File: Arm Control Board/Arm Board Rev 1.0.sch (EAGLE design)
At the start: 54 parts

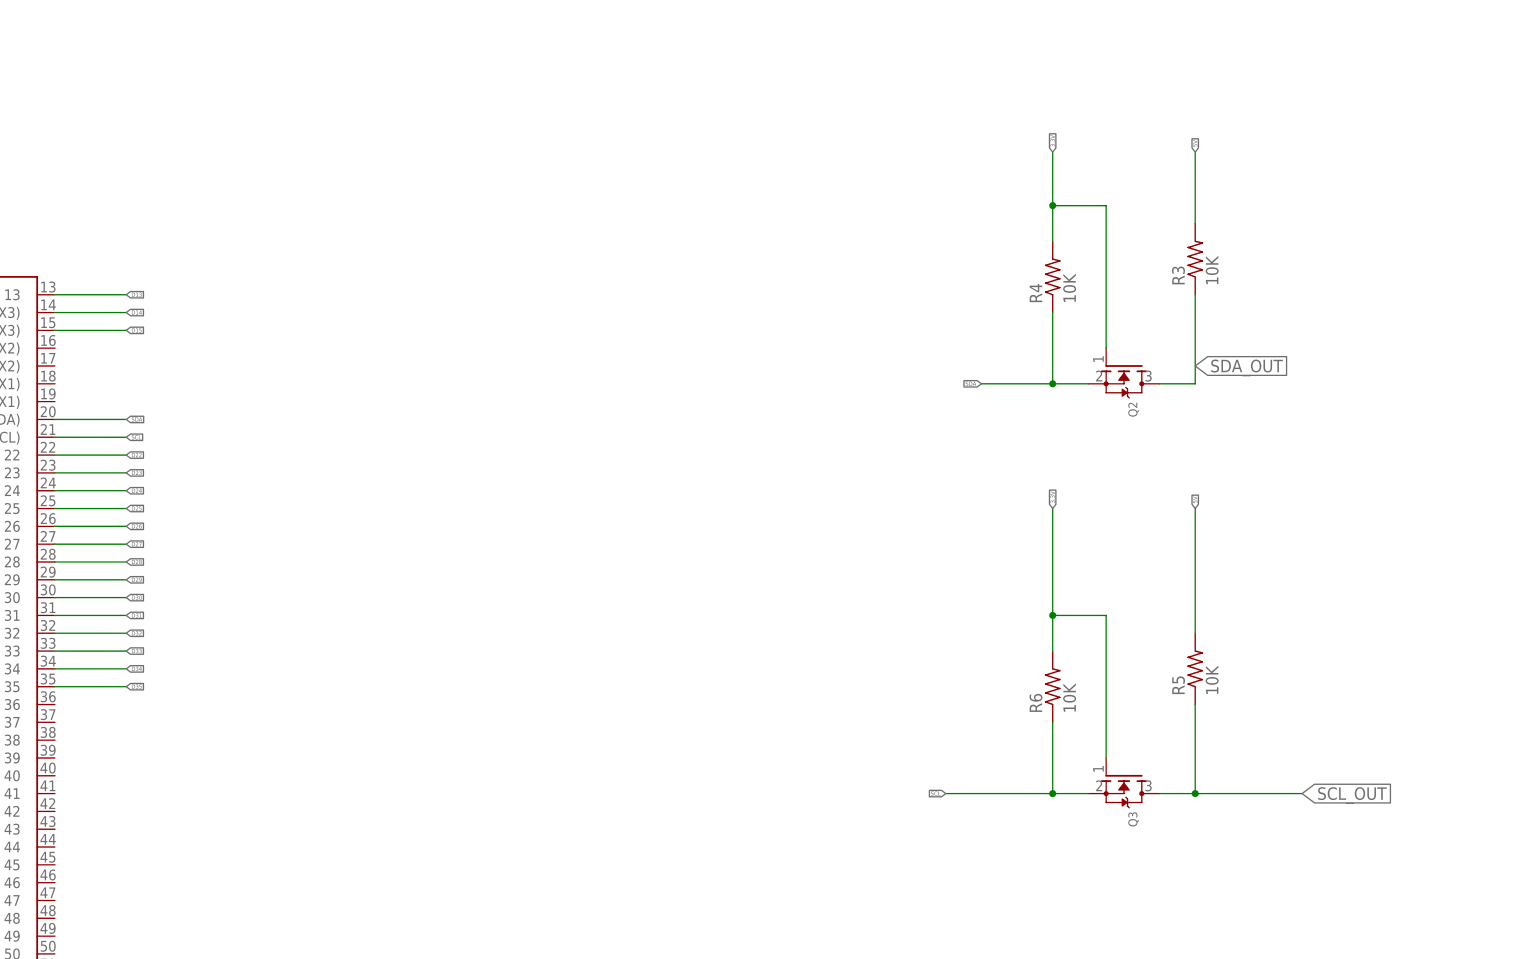
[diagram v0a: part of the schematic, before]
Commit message: added pull up resistors for i2c
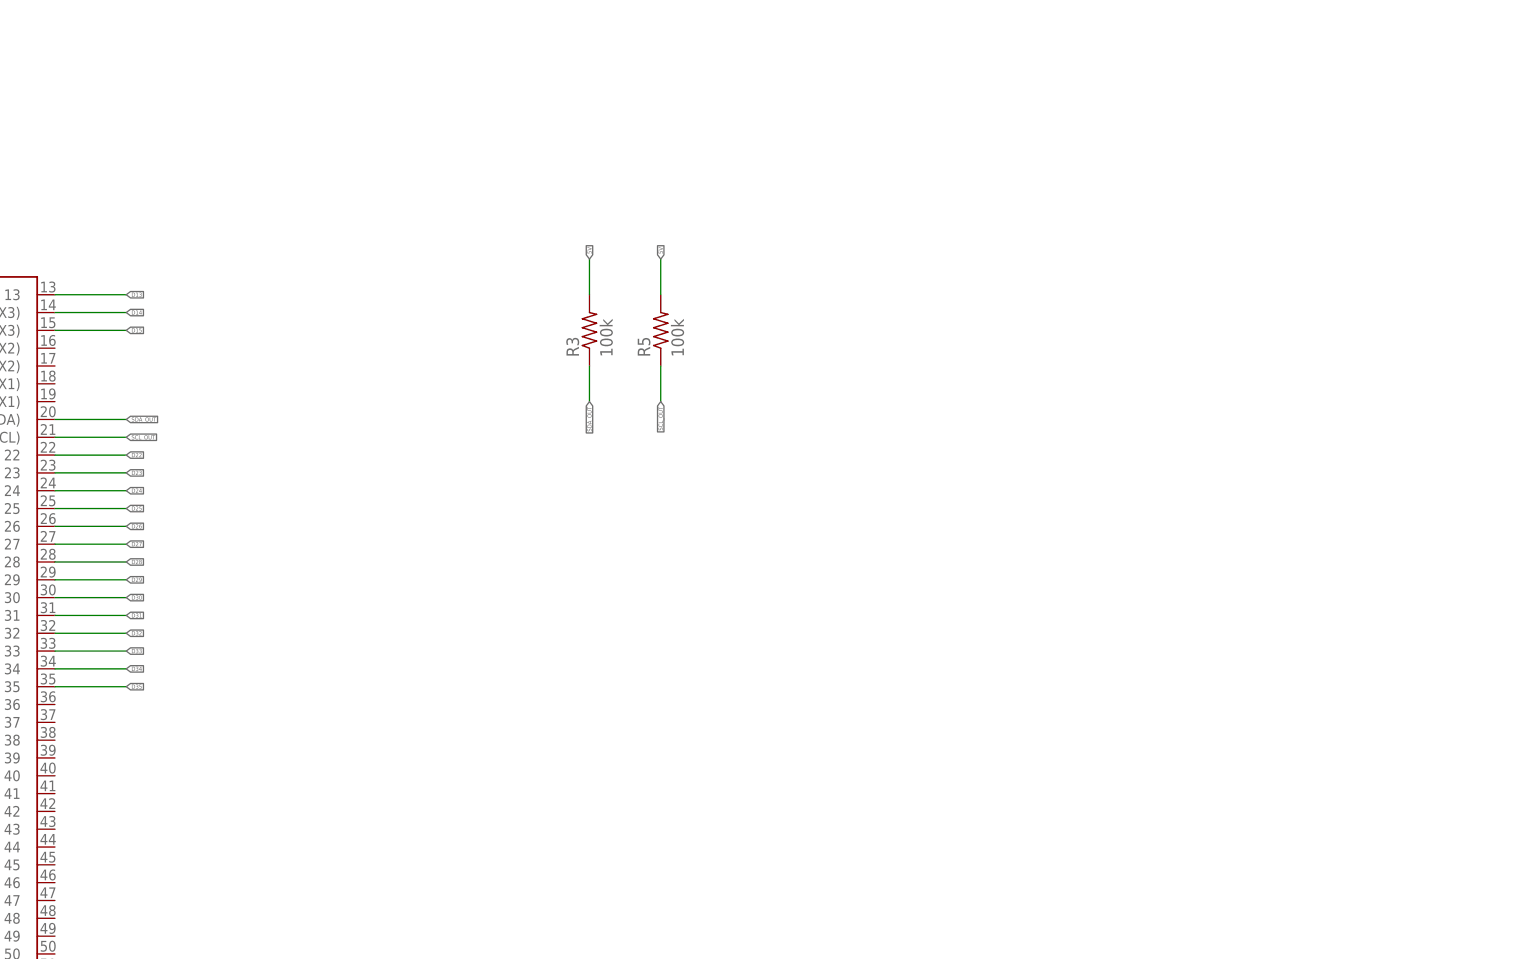
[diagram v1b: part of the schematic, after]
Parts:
- removed Q2, Q3: (no value), adafruit:MOSFET-NREFLOW
- removed R4, R6: 10K, rcl:R-US_R0603
- R3, R5: value 10K -> 100k; device rcl:R-US_R0603 -> rcl:R-US_0204/2V
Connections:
- removed net SCL: B1.21(SCL), Q3.S, R6.1
- removed net SDA: B1.20(SDA), Q2.S, R4.1
- net 3.3V: no longer Q2.G, Q3.G, R4.2, R6.2
- net SCL_OUT: now also B1.21(SCL); no longer Q3.D
- net SDA_OUT: now also B1.20(SDA); no longer Q2.D
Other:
- moved on the sheet: R3, R5

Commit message: removed tx and rx
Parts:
- removed Q13, Q14: (no value), adafruit:MOSFET-NREFLOW
- removed R25, R26, R27, R28: 10K, rcl:R-US_R0603
- removed RX: \, wirepad:3,81/1,1
- removed TX: (no value), wirepad:3,81/1,1
- R3, R5: value 100k -> 100K
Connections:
- removed net N$1: Q14.S, R28.1, RX.P
- removed net N$2: Q13.S, R26.1, TX.P
- net 3.3V: no longer Q13.G, Q14.G, R26.2, R28.2
- net 5V: no longer R25.2, R27.2
- net RX: no longer Q13.D, R25.1
- net TX: no longer Q14.D, R27.1
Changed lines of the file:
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@@
 </classes>
 <parts>
-<part name="TX" library="wirepad" deviceset="3,81/1,1" device=""/>
-<part name="RX" library="wirepad" deviceset="3,81/1,1" device="" value="\"/>
-<part name="Q13" library="adafruit" deviceset="MOSFET-N" device="REFLOW"/>
-<part name="R25" library="rcl" deviceset="R-US_" device="R0603" value="10K"/>
-<part name="R26" library="rcl" deviceset="R-US_" device="R0603" value="10K"/>
-<part name="Q14" library="adafruit" deviceset="MOSFET-N" device="REFLOW"/>
-<part name="R27" library="rcl" deviceset="R-US_" device="R0603" value="10K"/>
-<part name="R28" library="rcl" deviceset="R-US_" device="R0603" value="10K"/>
 <part name="12V" library="wirepad" deviceset="3,81/1,4" device=""/>
 <part name="GND" library="wirepad" deviceset="3,81/1,4" device=""/>
@@
 <part name="ENCODER_OUTPUT1" library="con-lstb" deviceset="MA04-1" device=""/>
 <part name="B1" library="SparkFun-Boards" library_urn="urn:adsk.eagle:library:509" deviceset="ARDUINO_MEGA_R3" device="FULL" package3d_urn="urn:adsk.eagle:package:37320/1"/>
-<part name="R3" library="rcl" library_urn="urn:adsk.eagle:library:334" deviceset="R-US_" device="0204/2V" package3d_urn="urn:adsk.eagle:package:23495/1" value="100k"/>
-<part name="R5" library="rcl" library_urn="urn:adsk.eagle:library:334" deviceset="R-US_" device="0204/2V" package3d_urn="urn:adsk.eagle:package:23495/1" value="100k"/>
+<part name="R3" library="rcl" library_urn="urn:adsk.eagle:library:334" deviceset="R-US_" device="0204/2V" package3d_urn="urn:adsk.eagle:package:23495/1" value="100K"/>
+<part name="R5" library="rcl" library_urn="urn:adsk.eagle:library:334" deviceset="R-US_" device="0204/2V" package3d_urn="urn:adsk.eagle:package:23495/1" value="100K"/>
 </parts>
 <sheets>
@@
 </plain>
 <instances>
-<instance part="TX" gate="P" x="25.4" y="60.96" smashed="yes">
-<attribute name="NAME" x="24.257" y="62.8142" size="1.778" layer="95"/>
-<attribute name="VALUE" x="24.257" y="57.658" size="1.778" layer="96"/>
-</instance>
-<instance part="RX" gate="P" x="25.4" y="33.02" smashed="yes">
-<attribute name="NAME" x="24.257" y="34.8742" size="1.778" layer="95"/>
-<attribute name="VALUE" x="24.257" y="29.718" size="1.778" layer="96"/>
-</instance>
-<instance part="Q13" gate="G$1" x="71.12" y="63.5" smashed="yes" rot="R270">
-<attribute name="NAME" x="71.755" y="58.42" size="1.27" layer="95" rot="R270"/>
-<attribute name="VALUE" x="69.85" y="58.42" size="1.27" layer="96" rot="R270"/>
-</instance>
-<instance part="R25" gate="G$1" x="81.28" y="78.74" smashed="yes" rot="R90">
-<attribute name="NAME" x="79.7814" y="74.93" size="1.778" layer="95" rot="R90"/>
-<attribute name="VALUE" x="84.582" y="74.93" size="1.778" layer="96" rot="R90"/>
-</instance>
-<instance part="R26" gate="G$1" x="60.96" y="76.2" smashed="yes" rot="R90">
-<attribute name="NAME" x="59.4614" y="72.39" size="1.778" layer="95" rot="R90"/>
-<attribute name="VALUE" x="64.262" y="72.39" size="1.778" layer="96" rot="R90"/>
-</instance>
-<instance part="Q14" gate="G$1" x="149.86" y="35.56" smashed="yes" rot="R270">
-<attribute name="NAME" x="150.495" y="30.48" size="1.27" layer="95" rot="R270"/>
-<attribute name="VALUE" x="148.59" y="30.48" size="1.27" layer="96" rot="R270"/>
-</instance>
-<instance part="R27" gate="G$1" x="160.02" y="50.8" smashed="yes" rot="R90">
-<attribute name="NAME" x="158.5214" y="46.99" size="1.778" layer="95" rot="R90"/>
-<attribute name="VALUE" x="163.322" y="46.99" size="1.778" layer="96" rot="R90"/>
-</instance>
-<instance part="R28" gate="G$1" x="139.7" y="48.26" smashed="yes" rot="R90">
-<attribute name="NAME" x="138.2014" y="44.45" size="1.778" layer="95" rot="R90"/>
-<attribute name="VALUE" x="143.002" y="44.45" size="1.778" layer="96" rot="R90"/>
-</instance>
 <instance part="12V" gate="1" x="0" y="342.9" smashed="yes">
 <attribute name="NAME" x="-1.143" y="344.7542" size="1.778" layer="95"/>
@@
 </busses>
 <nets>
-<net name="N$1" class="0">
-<segment>
-<pinref part="RX" gate="P" pin="P"/>
-<wire x1="27.94" y1="33.02" x2="139.7" y2="33.02" width="0.1524" layer="91"/>
-<pinref part="Q14" gate="G$1" pin="S"/>
-<pinref part="R28" gate="G$1" pin="1"/>
-<wire x1="139.7" y1="33.02" x2="144.78" y2="33.02" width="0.1524" layer="91"/>
-<wire x1="139.7" y1="43.18" x2="139.7" y2="33.02" width="0.1524" layer="91"/>
-<junction x="139.7" y="33.02"/>
-</segment>
-</net>
-<net name="N$2" class="0">
-<segment>
-<pinref part="Q13" gate="G$1" pin="S"/>
-<pinref part="TX" gate="P" pin="P"/>
-<wire x1="27.94" y1="60.96" x2="60.96" y2="60.96" width="0.1524" layer="91"/>
-<pinref part="R26" gate="G$1" pin="1"/>
-<wire x1="60.96" y1="60.96" x2="66.04" y2="60.96" width="0.1524" layer="91"/>
-<wire x1="60.96" y1="71.12" x2="60.96" y2="60.96" width="0.1524" layer="91"/>
-<junction x="60.96" y="60.96"/>
-</segment>
-</net>
 <net name="5V" class="0">
-<segment>
-<pinref part="R25" gate="G$1" pin="2"/>
-<wire x1="81.28" y1="83.82" x2="81.28" y2="99.06" width="0.1524" layer="91"/>
-<label x="81.28" y="99.06" size="0.6096" layer="95" rot="R90" xref="yes"/>
-</segment>
-<segment>
-<pinref part="R27" gate="G$1" pin="2"/>
-<wire x1="160.02" y1="55.88" x2="160.02" y2="71.12" width="0.1524" layer="91"/>
-<label x="160.02" y="71.12" size="0.6096" layer="95" rot="R90" xref="yes"/>
-</segment>
 <segment>
 <pinref part="ENCODER_OUTPUT" gate="1" pin="4"/>
@@
 </net>
 <net name="3.3V" class="0">
-<segment>
-<pinref part="Q13" gate="G$1" pin="G"/>
-<pinref part="R26" gate="G$1" pin="2"/>
-<wire x1="60.96" y1="86.36" x2="60.96" y2="81.28" width="0.1524" layer="91"/>
-<wire x1="68.58" y1="86.36" x2="60.96" y2="86.36" width="0.1524" layer="91"/>
-<wire x1="68.58" y1="86.36" x2="68.58" y2="66.04" width="0.1524" layer="91"/>
-<wire x1="60.96" y1="86.36" x2="60.96" y2="99.06" width="0.1524" layer="91"/>
-<junction x="60.96" y="86.36"/>
-<label x="60.96" y="99.06" size="0.6096" layer="95" rot="R90" xref="yes"/>
-</segment>
-<segment>
-<pinref part="Q14" gate="G$1" pin="G"/>
-<pinref part="R28" gate="G$1" pin="2"/>
-<wire x1="139.7" y1="58.42" x2="139.7" y2="53.34" width="0.1524" layer="91"/>
-<wire x1="147.32" y1="58.42" x2="139.7" y2="58.42" width="0.1524" layer="91"/>
-<wire x1="147.32" y1="58.42" x2="147.32" y2="38.1" width="0.1524" layer="91"/>
-<wire x1="139.7" y1="58.42" x2="139.7" y2="71.12" width="0.1524" layer="91"/>
-<junction x="139.7" y="58.42"/>
-<label x="139.7" y="71.12" size="0.6096" layer="95" rot="R90" xref="yes"/>
-</segment>
 <segment>
 <wire x1="647.7" y1="259.08" x2="685.8" y2="259.08" width="0.1524" layer="91"/>
@@
 <net name="RX" class="0">
 <segment>
-<pinref part="Q13" gate="G$1" pin="D"/>
-<wire x1="76.2" y1="60.96" x2="81.28" y2="60.96" width="0.1524" layer="91"/>
-<pinref part="R25" gate="G$1" pin="1"/>
-<wire x1="81.28" y1="73.66" x2="81.28" y2="60.96" width="0.1524" layer="91"/>
-<wire x1="81.28" y1="60.96" x2="121.92" y2="60.96" width="0.1524" layer="91"/>
-<junction x="81.28" y="60.96"/>
-<label x="121.92" y="60.96" size="0.6096" layer="95" xref="yes"/>
-</segment>
-<segment>
 <pinref part="B1" gate="G$1" pin="0(RX0)"/>
 <wire x1="322.58" y1="121.92" x2="312.42" y2="121.92" width="0.1524" layer="91"/>
@@
 <net name="TX" class="0">
 <segment>
-<pinref part="R27" gate="G$1" pin="1"/>
-<wire x1="160.02" y1="45.72" x2="160.02" y2="33.02" width="0.1524" layer="91"/>
-<wire x1="160.02" y1="33.02" x2="182.88" y2="33.02" width="0.1524" layer="91"/>
-<junction x="160.02" y="33.02"/>
-<pinref part="Q14" gate="G$1" pin="D"/>
-<wire x1="154.94" y1="33.02" x2="160.02" y2="33.02" width="0.1524" layer="91"/>
-<label x="182.88" y="33.02" size="0.6096" layer="95" xref="yes"/>
-</segment>
-<segment>
 <pinref part="B1" gate="G$1" pin="1(TX0)"/>
